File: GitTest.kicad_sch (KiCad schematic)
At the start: 0 parts

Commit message: Add a cap
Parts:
- added C?: C, symbol Device:C
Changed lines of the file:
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@@
 	(generator_version "10.0")
 	(paper "A4")
+	(symbol
+		(lib_id "Device:C")
+		(at 105.41 60.96 0)
+		(unit 1)
+		(body_style 1)
+		(exclude_from_sim no)
+		(in_bom yes)
+		(on_board yes)
+		(in_pos_files yes)
+		(dnp no)
+		(fields_autoplaced yes)
+		(property "Reference" "C?"
+			(at 109.22 59.6899 0)
+			(show_name no)
+			(do_not_autoplace no)
+			(effects
+				(font
+					(size 1.27 1.27)
+				)
+				(justify left)
+			)
+		)
+		(property "Value" "C"
+			(at 109.22 62.2299 0)
+			(show_name no)
+			(do_not_autoplace no)
+			(effects
+				(font
+					(size 1.27 1.27)
+				)
+				(justify left)
+			)
+		)
+		(property "Footprint" ""
+			(at 106.3752 64.77 0)
+			(hide yes)
+			(show_name no)
+			(do_not_autoplace no)
+			(effects
+				(font
+					(size 1.27 1.27)
+				)
+			)
+		)
+		(property "Datasheet" ""
+			(at 105.41 60.96 0)
+			(hide yes)
+			(show_name no)
+			(do_not_autoplace no)
+			(effects
+				(font
+					(size 1.27 1.27)
+				)
+			)
+		)
+		(property "Description" "Unpolarized capacitor"
+			(at 105.41 60.96 0)
+			(hide yes)
+			(show_name no)
+			(do_not_autoplace no)
+			(effects
+				(font
+					(size 1.27 1.27)
+				)
+			)
+		)
+		(pin "2"
+		)
+		(pin "1"
+		)
+		(instances
+			(project "GitTest"
+				(path "/b547b56b-9bed-4878-9909-a8b350d373a3"
+					(reference "C?")
+					(unit 1)
+				)
+			)
+		)
+	)
 	(sheet_instances
 		(path "/"

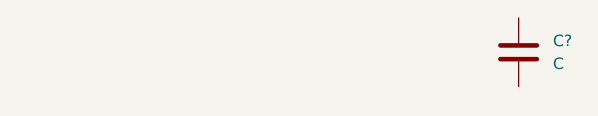
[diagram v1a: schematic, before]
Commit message: Add second capacitor
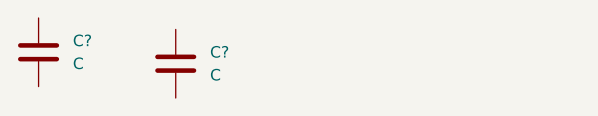
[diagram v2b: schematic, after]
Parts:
- added C?: C, symbol Device:C
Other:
- moved on the sheet: C?
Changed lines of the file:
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@@
 	(symbol
 		(lib_id "Device:C")
-		(at 105.41 60.96 0)
+		(at 52.07 60.96 0)
 		(unit 1)
 		(body_style 1)
@@
 		(fields_autoplaced yes)
 		(property "Reference" "C?"
-			(at 109.22 59.6899 0)
+			(at 55.88 59.6899 0)
 			(show_name no)
 			(do_not_autoplace no)
@@
 		)
 		(property "Value" "C"
-			(at 109.22 62.2299 0)
+			(at 55.88 62.2299 0)
 			(show_name no)
 			(do_not_autoplace no)
@@
 		)
 		(property "Footprint" ""
-			(at 106.3752 64.77 0)
+			(at 53.0352 64.77 0)
 			(hide yes)
 			(show_name no)
@@
 		)
 		(property "Datasheet" ""
-			(at 105.41 60.96 0)
+			(at 52.07 60.96 0)
 			(hide yes)
 			(show_name no)
@@
 		)
 		(property "Description" "Unpolarized capacitor"
-			(at 105.41 60.96 0)
+			(at 52.07 60.96 0)
 			(hide yes)
 			(show_name no)
@@
 		)
 		(instances
+			(project "GitTest"
+				(path "/b547b56b-9bed-4878-9909-a8b350d373a3"
+					(reference "C?")
+					(unit 1)
+				)
+			)
+		)
+	)
+	(symbol
+		(lib_id "Device:C")
+		(at 67.31 62.23 0)
+		(unit 1)
+		(body_style 1)
+		(exclude_from_sim no)
+		(in_bom yes)
+		(on_board yes)
+		(in_pos_files yes)
+		(dnp no)
+		(fields_autoplaced yes)
+		(property "Reference" "C?"
+			(at 71.12 60.9599 0)
+			(show_name no)
+			(do_not_autoplace no)
+			(effects
+				(font
+					(size 1.27 1.27)
+				)
+				(justify left)
+			)
+		)
+		(property "Value" "C"
+			(at 71.12 63.4999 0)
+			(show_name no)
+			(do_not_autoplace no)
+			(effects
+				(font
+					(size 1.27 1.27)
+				)
+				(justify left)
+			)
+		)
+		(property "Footprint" ""
+			(at 68.2752 66.04 0)
+			(hide yes)
+			(show_name no)
+			(do_not_autoplace no)
+			(effects
+				(font
+					(size 1.27 1.27)
+				)
+			)
+		)
+		(property "Datasheet" ""
+			(at 67.31 62.23 0)
+			(hide yes)
+			(show_name no)
+			(do_not_autoplace no)
+			(effects
+				(font
+					(size 1.27 1.27)
+				)
+			)
+		)
+		(property "Description" "Unpolarized capacitor"
+			(at 67.31 62.23 0)
+			(hide yes)
+			(show_name no)
+			(do_not_autoplace no)
+			(effects
+				(font
+					(size 1.27 1.27)
+				)
+			)
+		)
+		(pin "1"
+		)
+		(pin "2"
+		)
+		(instances

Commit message: Change to LED an battery
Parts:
- removed C? (x2): C, symbol Device:C
- added BT?: Battery_Cell, symbol Device:Battery_Cell
- added D?: LED, symbol Device:LED
- added R?: R, symbol Device:R
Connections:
- new net: D?.2 (A), R?.2
- new net: BT?.1 (+), R?.1
- new net GND: BT?.2 (-), D?.1 (K)
